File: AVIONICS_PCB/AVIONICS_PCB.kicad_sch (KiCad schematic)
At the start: 3 parts, among them J1 Conn_01x06, J2 Conn_01x04, U1 XIAO-ESP32-S3-DIP

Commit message: changes to schematic
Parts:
- added ACCELEROMETER: Conn_01x08, Connector_PinHeader_2.54mm:PinHeader_1x08_P2.54mm_Vertical, symbol Connector_Generic:Conn_01x08
- added ALTITUDE: Conn_01x04, Connector_PinHeader_2.54mm:PinHeader_1x04_P2.54mm_Vertical, symbol Connector_Generic:Conn_01x04
- renumbered J2 to GPS, J1 to SD_READER
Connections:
- net +3V3: now also SD_READER.6 (Pin_6), ALTITUDE.1 (Pin_1); no longer SD_READER.1 (Pin_1)
- net +5V: now also ACCELEROMETER.1 (Pin_1)
- net CLK: now also U1.9 (PA7_A8_D8_SCK)
- net CS: now also U1.4 (PA11_A3_D3)
- net GND: now also SD_READER.1 (Pin_1), ACCELEROMETER.2 (Pin_2), ALTITUDE.2 (Pin_2); no longer SD_READER.6 (Pin_6)
- net MISO: now also U1.10 (PA5_A9_D9_MISO)
- net MOSI: now also U1.11 (PA6_A10_D10_MOSI)
- net SDA: now reaches U1.5 (PA8_A4_D4_SDA)
- net SDA: now also ACCELEROMETER.4 (Pin_4), ALTITUDE.4 (Pin_4)
- net SCL: now reaches U1.6 (PA9_A5_D5_SCL)
- net SCL: now also ACCELEROMETER.3 (Pin_3), ALTITUDE.3 (Pin_3)

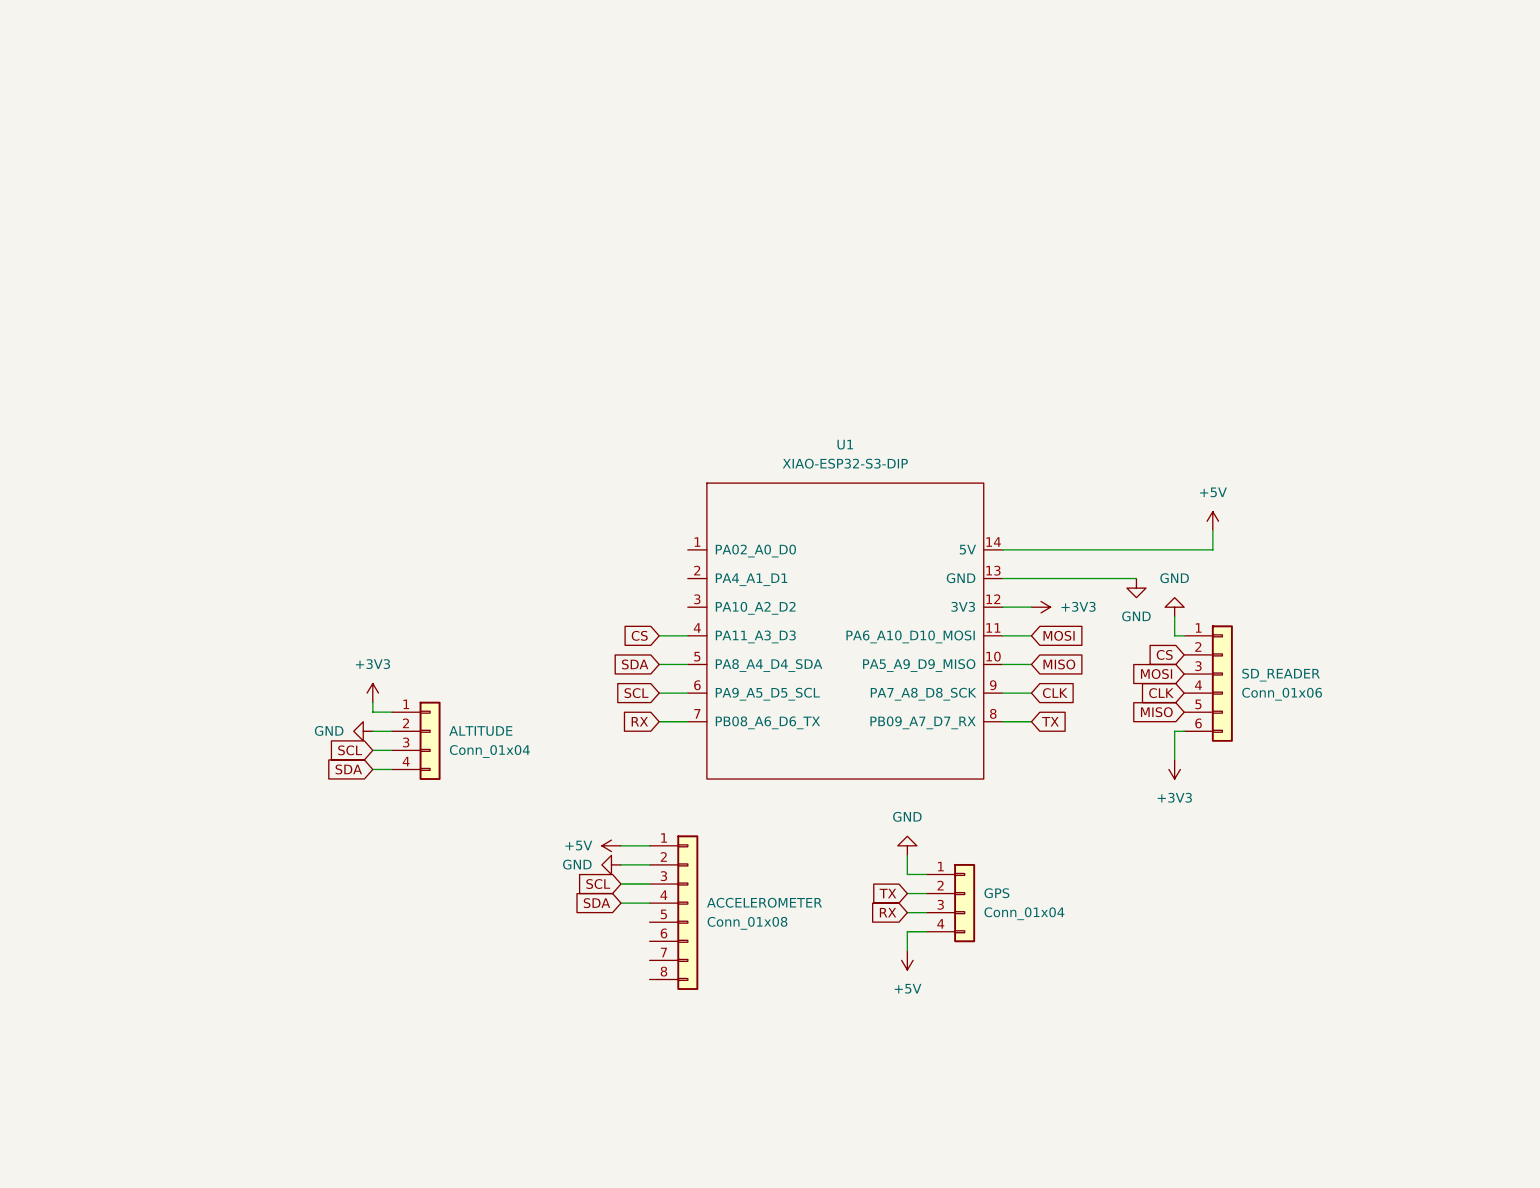
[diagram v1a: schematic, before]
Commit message: Started layout
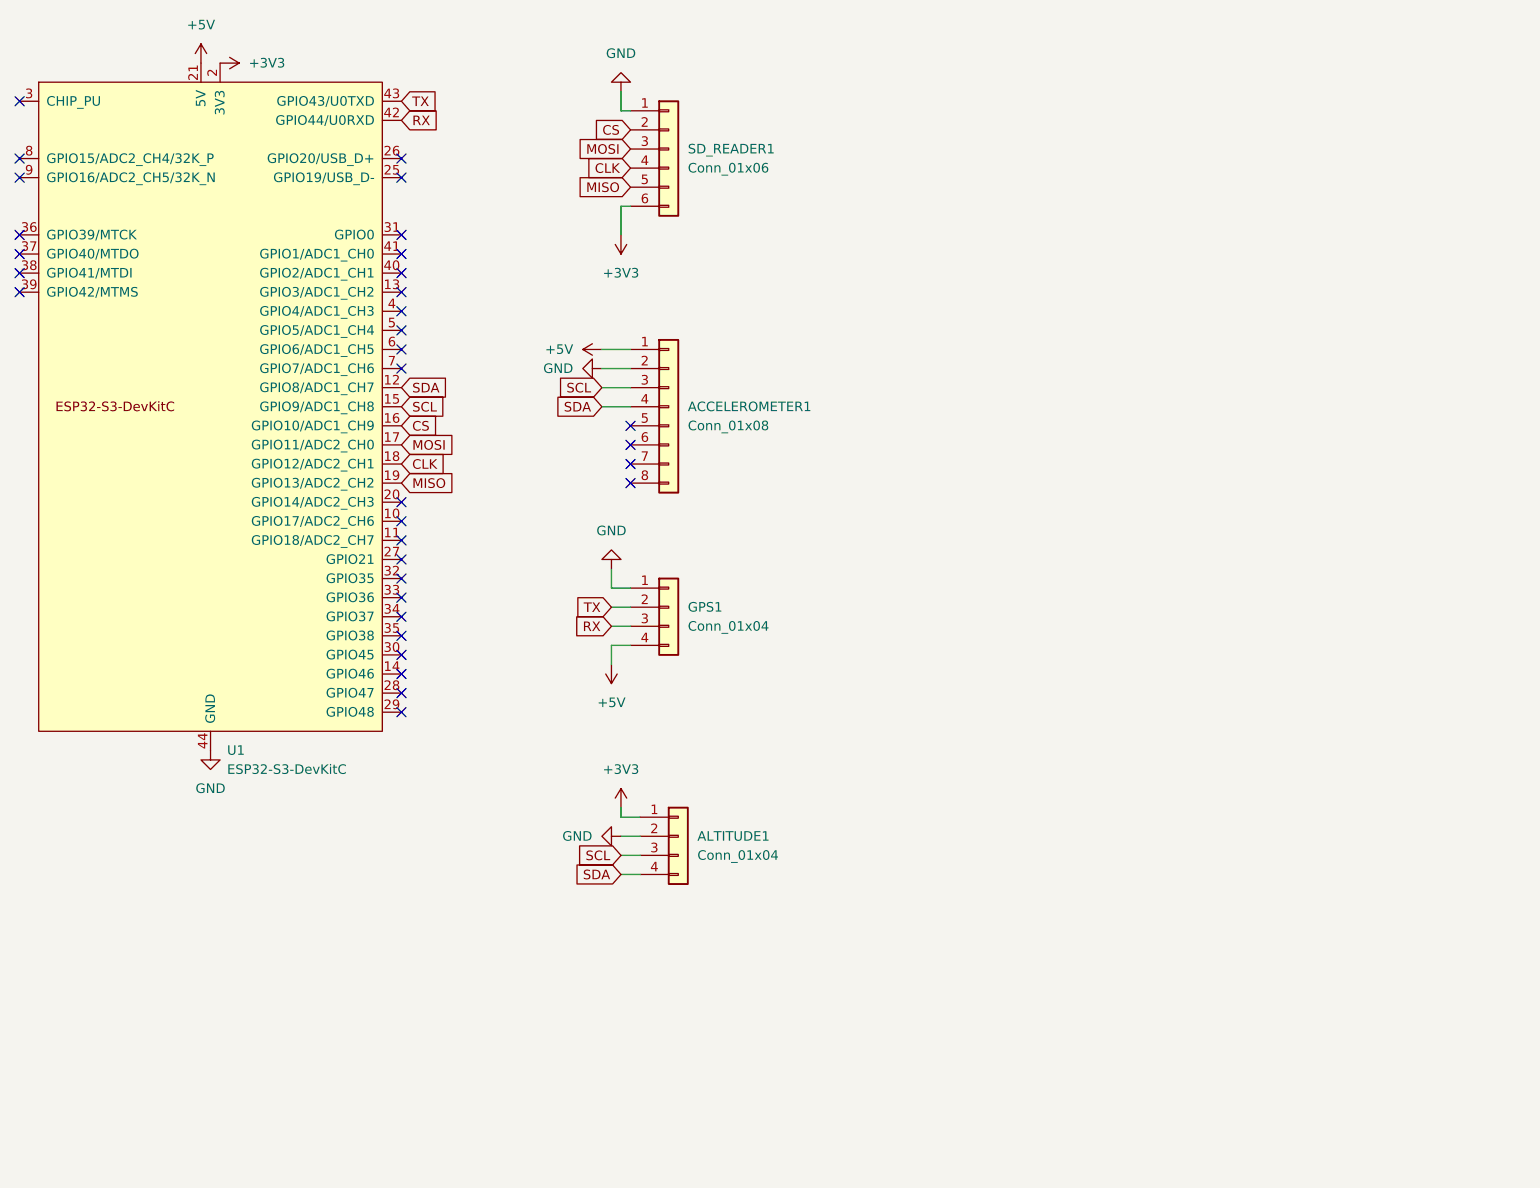
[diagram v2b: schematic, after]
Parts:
- removed U1: XIAO-ESP32-S3-DIP, symbol Seeed_Studio_XIAO_Series-20240814:XIAO-ESP32-S3-DIP
- added U1: ESP32-S3-DevKitC, PCM_Espressif:ESP32-S3-DevKitC, symbol PCM_Espressif:ESP32-S3-DevKitC
- renumbered ACCELEROMETER to ACCELEROMETER1, ALTITUDE to ALTITUDE1, GPS to GPS1, SD_READER to SD_READER1
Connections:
- net +3V3: now also U1.1 (3V3), U1.2 (3V3)
- net +5V: now also U1.21 (5V)
- net CLK: now also U1.18 (GPIO12/ADC2_CH1)
- net CS: now also U1.16 (GPIO10/ADC1_CH9)
- net GND: now also U1.22 (GND), U1.23 (GND), U1.24 (GND), U1.44 (GND)
- net MISO: now also U1.19 (GPIO13/ADC2_CH2)
- net MOSI: now also U1.17 (GPIO11/ADC2_CH0)
- net RX: now also U1.42 (GPIO44/U0RXD)
- net SCL: now also U1.15 (GPIO9/ADC1_CH8)
- net SDA: now also U1.12 (GPIO8/ADC1_CH7)
- net TX: now also U1.43 (GPIO43/U0TXD)
- no-connect marks 0 -> 33
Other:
- moved on the sheet: ACCELEROMETER1, ALTITUDE1, GPS1, SD_READER1

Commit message: Added power system
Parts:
- added C1: C, Capacitor_SMD:C_0805_2012Metric_Pad1.18x1.45mm_HandSolder, symbol Device:C
- added CR1: LD1117V33, TO-220_STM, symbol LD117V33:LD1117V33
- added J1: XT30PW-M, XT30PW-M:AMASS_XT30PW-M, symbol XT30PW-M:XT30PW-M
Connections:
- net +3V3: now also CR1.2 (VOUT)
- net GND: now also C1.2, CR1.1 (ADJ/GND), J1.N
- new net: C1.1, CR1.3 (VIN), J1.P

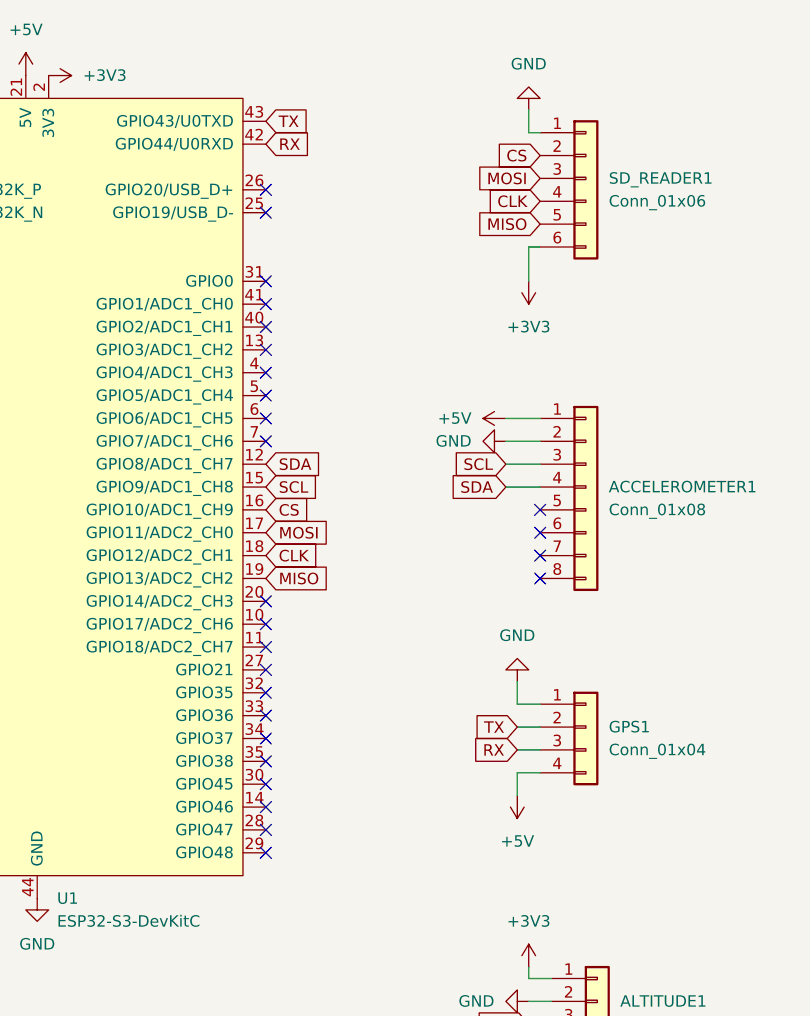
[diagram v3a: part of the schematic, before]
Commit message: Got sensors in right configuration
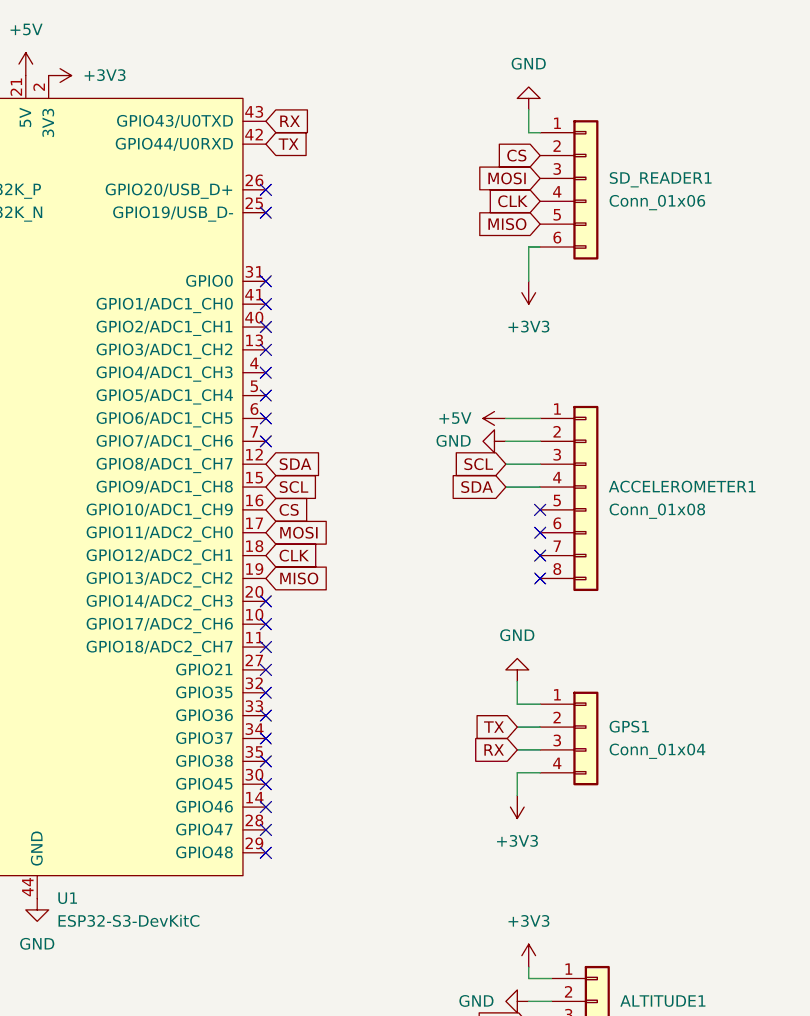
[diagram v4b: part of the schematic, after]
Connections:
- net +3V3: now also GPS1.4 (Pin_4)
- net +5V: no longer GPS1.4 (Pin_4)
- net RX: now also U1.43 (GPIO43/U0TXD); no longer U1.42 (GPIO44/U0RXD)
- net TX: now also U1.42 (GPIO44/U0RXD); no longer U1.43 (GPIO43/U0TXD)
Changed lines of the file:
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@@
 	(global_label "TX"
 		(shape input)
-		(at 77.47 22.86 0)
+		(at 77.47 25.4 0)
 		(fields_autoplaced yes)
 		(effects
@@
 		)
 		(property "Intersheetrefs" "${INTERSHEET_REFS}"
-			(at 82.6323 22.86 0)
+			(at 82.6323 25.4 0)
 			(effects
 				(font
@@
 	(global_label "RX"
 		(shape input)
-		(at 77.47 25.4 0)
+		(at 77.47 22.86 0)
 		(fields_autoplaced yes)
 		(effects
@@
 		)
 		(property "Intersheetrefs" "${INTERSHEET_REFS}"
-			(at 82.9347 25.4 0)
+			(at 82.9347 22.86 0)
 			(effects
 				(font
@@
 	)
 	(symbol
-		(lib_id "power:+5V")
+		(lib_id "power:GND")
+		(at 52.07 109.22 0)
+		(unit 1)
+		(exclude_from_sim no)
+		(in_bom yes)
+		(on_board yes)
+		(dnp no)
+		(fields_autoplaced yes)
+		(property "Reference" "#PWR01"
+			(at 52.07 115.57 0)
+			(effects
+				(font
+					(size 1.27 1.27)
+				)
+				(hide yes)
+			)
+		)
+		(property "Value" "GND"
+			(at 52.07 114.3 0)
+			(effects
+				(font
+					(size 1.27 1.27)
+				)
+			)
+		)
+		(property "Footprint" ""
+			(at 52.07 109.22 0)
+			(effects
+				(font
+					(size 1.27 1.27)
+				)
+				(hide yes)
+			)
+		)
+		(property "Datasheet" ""
+			(at 52.07 109.22 0)
+			(effects
+				(font
+					(size 1.27 1.27)
+				)
+				(hide yes)
+			)
+		)
+		(property "Description" "Power symbol creates a global label with name \"GND\" , ground"
+			(at 52.07 109.22 0)
+			(effects
+				(font
+					(size 1.27 1.27)
+				)
+				(hide yes)
+			)
+		)
+		(pin "1"
+		)
+		(instances
+			(project "AVIONICS_PCB"
+				(path "/62770ac1-9b47-4d00-b615-ae949e917d5b"
+					(reference "#PWR01")
+					(unit 1)
+				)
+			)
+		)
+	)
+	(symbol
+		(lib_id "power:+3V3")
+		(at 53.34 17.78 270)
+		(unit 1)
+		(exclude_from_sim no)
+		(in_bom yes)
+		(on_board yes)
+		(dnp no)
+		(fields_autoplaced yes)
+		(property "Reference" "#PWR06"
+			(at 49.53 17.78 0)
+			(effects
+				(font
+					(size 1.27 1.27)
+				)
+				(hide yes)
+			)
+		)
+		(property "Value" "+3V3"
+			(at 57.15 17.7799 90)
+			(effects
+				(font
+					(size 1.27 1.27)
+				)
+				(justify left)
+			)
+		)
+		(property "Footprint" ""
+			(at 53.34 17.78 0)
+			(effects
+				(font
+					(size 1.27 1.27)
+				)
+				(hide yes)
+			)
+		)
+		(property "Datasheet" ""
+			(at 53.34 17.78 0)
+			(effects
+				(font
+					(size 1.27 1.27)
+				)
+				(hide yes)
+			)
+		)
+		(property "Description" "Power symbol creates a global label with name \"+3V3\""
+			(at 53.34 17.78 0)
+			(effects
+				(font
+					(size 1.27 1.27)
+				)
+				(hide yes)
+			)
+		)
+		(pin "1"
+		)
+		(instances
+			(project "AVIONICS_PCB"
+				(path "/62770ac1-9b47-4d00-b615-ae949e917d5b"
+					(reference "#PWR06")
+					(unit 1)
+				)
+			)
+		)
+	)
+	(symbol
+		(lib_id "power:+3V3")
 		(at 105.41 97.79 180)
 		(unit 1)
@@
 			)
 		)
-		(property "Value" "+5V"
+		(property "Value" "+3V3"
 			(at 105.41 102.87 0)
 			(effects
@@
 			)
 		)
-		(property "Description" "Power symbol creates a global label with name \"+5V\""
+		(property "Description" "Power symbol creates a global label with name \"+3V3\""
 			(at 105.41 97.79 0)
 			(effects
@@
 					(unit 1)
 				)
-			)
-		)
-	)
-	(symbol
-		(lib_id "power:GND")
-		(at 52.07 109.22 0)
-		(unit 1)
-		(exclude_from_sim no)
-		(in_bom yes)
-		(on_board yes)
-		(dnp no)
-		(fields_autoplaced yes)
-		(property "Reference" "#PWR01"
-			(at 52.07 115.57 0)
-			(effects
-				(font
-					(size 1.27 1.27)
-				)
-				(hide yes)
-			)
-		)
-		(property "Value" "GND"
-			(at 52.07 114.3 0)
-			(effects
-				(font
-					(size 1.27 1.27)
-				)
-			)
-		)
-		(property "Footprint" ""
-			(at 52.07 109.22 0)
-			(effects
-				(font
-					(size 1.27 1.27)
-				)
-				(hide yes)
-			)
-		)
-		(property "Datasheet" ""
-			(at 52.07 109.22 0)
-			(effects
-				(font
-					(size 1.27 1.27)
-				)
-				(hide yes)
-			)
-		)
-		(property "Description" "Power symbol creates a global label with name \"GND\" , ground"
-			(at 52.07 109.22 0)
-			(effects
-				(font
-					(size 1.27 1.27)
-				)
-				(hide yes)
-			)
-		)
-		(pin "1"
-		)
-		(instances
-			(project "AVIONICS_PCB"
-				(path "/62770ac1-9b47-4d00-b615-ae949e917d5b"
-					(reference "#PWR01")
-					(unit 1)
-				)
-			)
-		)
-	)
-	(symbol
-		(lib_id "power:+3V3")
-		(at 53.34 17.78 270)
-		(unit 1)
-		(exclude_from_sim no)
-		(in_bom yes)
-		(on_board yes)
-		(dnp no)
-		(fields_autoplaced yes)
-		(property "Reference" "#PWR06"
-			(at 49.53 17.78 0)
-			(effects
-				(font
-					(size 1.27 1.27)
-				)
-				(hide yes)
-			)
-		)
-		(property "Value" "+3V3"
-			(at 57.15 17.7799 90)
-			(effects
-				(font
-					(size 1.27 1.27)
-				)
-				(justify left)
-			)
-		)
-		(property "Footprint" ""
-			(at 53.34 17.78 0)
-			(effects
-				(font
-					(size 1.27 1.27)
-				)
-				(hide yes)
-			)
-		)
-		(property "Datasheet" ""
-			(at 53.34 17.78 0)
-			(effects
-				(font
-					(size 1.27 1.27)
-				)
-				(hide yes)
-			)
-		)
-		(property "Description" "Power symbol creates a global label with name \"+3V3\""
-			(at 53.34 17.78 0)
-			(effects
-				(font
-					(size 1.27 1.27)
-				)
-				(hide yes)
-			)
-		)
-		(pin "1"
-		)
-		(instances
-			(project "AVIONICS_PCB"
-				(path "/62770ac1-9b47-4d00-b615-ae949e917d5b"
-					(reference "#PWR06")
-					(unit 1)
-				)
